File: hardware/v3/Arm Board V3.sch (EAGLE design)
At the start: 75 parts, among them CN1 1X4-BIG, IC1 L6206D, IC2 L6206D, IC3 L6206D, IC4 7812TV, IC5 7812TV, IC6 7812TV, IC7 7812DT, IC9 7812DT, Q3 Q_LTC490, U1 MAX3468CPA, U2 XBEE-1B3

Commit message: Created and populated BOM
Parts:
- C12: device SparkFun-Capacitors:CAPKIT -> SparkFun-Capacitors:0.1UF-25V-5%(0603)
- R9: device SparkFun-Passives:RESISTOR0805-RES -> SparkFun-Passives:RESISTOR0603-RES
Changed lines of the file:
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@@
 <part name="GND53" library="SparkFun-Aesthetics" deviceset="GND" device=""/>
 <part name="GND54" library="SparkFun-Aesthetics" deviceset="GND" device=""/>
-<part name="R9" library="SparkFun-Passives" deviceset="RESISTOR" device="0805-RES" value="220"/>
+<part name="R9" library="SparkFun-Passives" deviceset="RESISTOR" device="0603-RES" value="220"/>
 <part name="U$1" library="StellarisLaunchPad_Fred" deviceset="STELLARIS-LAUNCHPAD" device="STELLARIS-LAUNCHPAD-XL"/>
 <part name="U$3" library="SparkFun-Connectors" deviceset="RJ45-8" device="PTH"/>
@@
 <part name="Q3" library="PCB0M1" deviceset="Q_LTC490" device=""/>
 <part name="R11" library="SparkFun-Passives" deviceset="RESISTOR" device="0603-RES" value="120 Ohm"/>
-<part name="C12" library="SparkFun-Capacitors" deviceset="CAP" device="KIT" value=".1uF"/>
+<part name="C12" library="SparkFun-Capacitors" deviceset="0.1UF-25V-5%(0603)" device="" value=".1uF"/>
 <part name="GND8" library="SparkFun-Aesthetics" deviceset="GND" device=""/>
 <part name="H1" library="Lib_TH" deviceset="H_MNTHOLE" device="_#4"/>

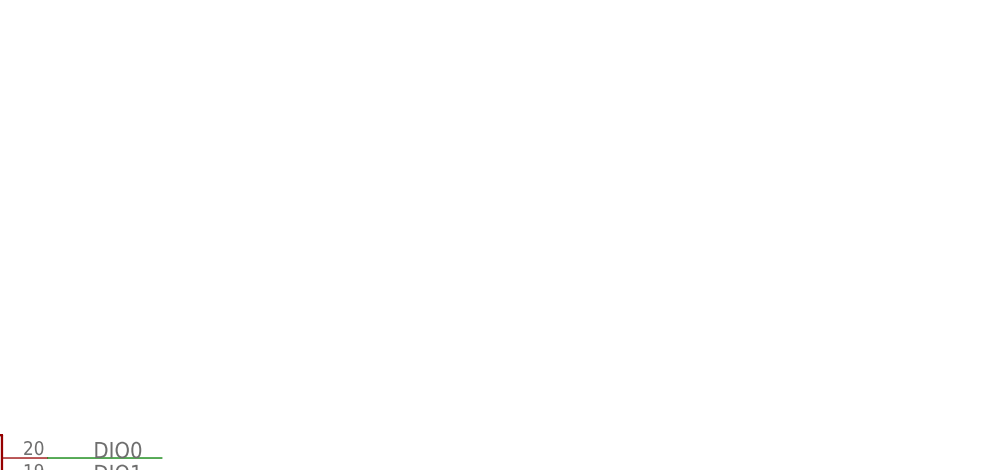
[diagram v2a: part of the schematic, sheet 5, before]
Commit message: Added RS485 jack next to Xbee
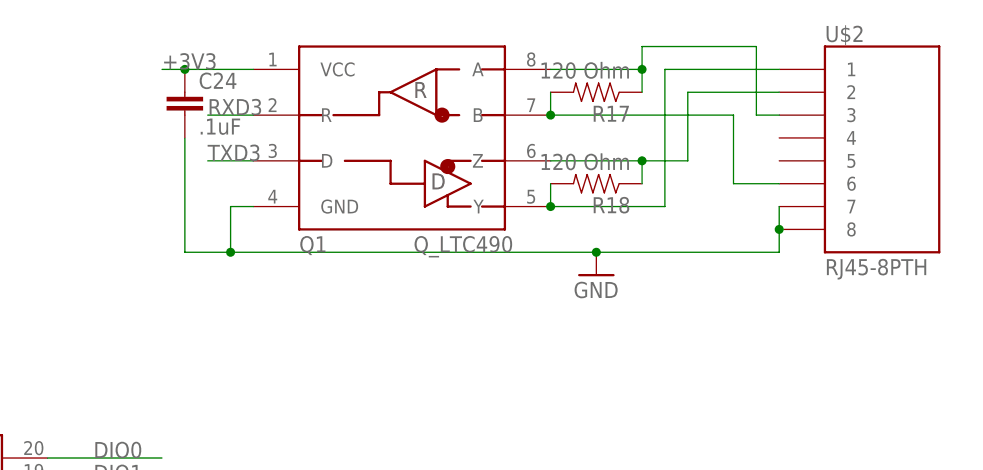
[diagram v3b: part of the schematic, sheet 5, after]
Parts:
- added C24: .1uF, SparkFun-Capacitors:0.1UF-25V-5%(0603)
- added Q1: Q_LTC490, PCB0M1:Q_LTC490
- added R17, R18: 120 Ohm, SparkFun-Passives:RESISTOR0603-RES
- added U$2: RJ45-8PTH, SparkFun-Connectors:RJ45-8PTH
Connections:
- new net N$12: Q1.Y, R18.2, U$2.1
- new net N$14: Q1.Z, R18.1, U$2.2
- new net N$20: Q1.B, R17.2, U$2.6
- new net N$21: Q1.A, R17.1, U$2.3
- net +3V3: now also C24.1, Q1.VCC
- net GND: now also C24.2, Q1.GND, U$2.7, U$2.8
- net RXD3: now also Q1.R
- net TXD3: now also Q1.D
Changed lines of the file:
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@@
 <part name="C23" library="SparkFun-Capacitors" deviceset="0.1UF-25V(+80/-20%)(0603)" device="" value="0.1uF"/>
 <part name="IC9" library="linear" deviceset="78*" device="DT" technology="12" value="7812DT"/>
+<part name="U$2" library="SparkFun-Connectors" deviceset="RJ45-8" device="PTH"/>
+<part name="R17" library="SparkFun-Passives" deviceset="RESISTOR" device="0603-RES" value="120 Ohm"/>
+<part name="GND25" library="supply1" deviceset="GND" device=""/>
+<part name="Q1" library="PCB0M1" deviceset="Q_LTC490" device=""/>
+<part name="R18" library="SparkFun-Passives" deviceset="RESISTOR" device="0603-RES" value="120 Ohm"/>
+<part name="C24" library="SparkFun-Capacitors" deviceset="0.1UF-25V-5%(0603)" device="" value=".1uF"/>
 </parts>
 <sheets>
@@
 <instance part="R16" gate="G$1" x="55.88" y="63.5" rot="R90"/>
 <instance part="GND31" gate="1" x="55.88" y="43.18"/>
+<instance part="U$2" gate="G$1" x="162.56" y="58.42"/>
+<instance part="R17" gate="G$1" x="129.54" y="66.04" rot="R180"/>
+<instance part="GND25" gate="1" x="129.54" y="45.72"/>
+<instance part="Q1" gate="G$1" x="99.06" y="58.42"/>
+<instance part="R18" gate="G$1" x="129.54" y="55.88" rot="R180"/>
+<instance part="C24" gate="G$1" x="83.82" y="63.5"/>
 </instances>
 <busses>
@@
 <wire x1="27.94" y1="2.54" x2="2.54" y2="2.54" width="0.1524" layer="91"/>
 </segment>
+<segment>
+<pinref part="GND25" gate="1" pin="GND"/>
+<wire x1="88.9" y1="48.26" x2="129.54" y2="48.26" width="0.1524" layer="91"/>
+<pinref part="Q1" gate="G$1" pin="GND"/>
+<wire x1="88.9" y1="48.26" x2="88.9" y2="53.34" width="0.1524" layer="91"/>
+<wire x1="88.9" y1="53.34" x2="91.44" y2="53.34" width="0.1524" layer="91"/>
+<junction x="129.54" y="48.26"/>
+<pinref part="C24" gate="G$1" pin="2"/>
+<wire x1="83.82" y1="60.96" x2="83.82" y2="48.26" width="0.1524" layer="91"/>
+<wire x1="83.82" y1="48.26" x2="88.9" y2="48.26" width="0.1524" layer="91"/>
+<junction x="88.9" y="48.26"/>
+<pinref part="U$2" gate="G$1" pin="8"/>
+<pinref part="U$2" gate="G$1" pin="7"/>
+<wire x1="149.86" y1="53.34" x2="149.86" y2="50.8" width="0.1524" layer="91"/>
+<junction x="149.86" y="50.8"/>
+<wire x1="149.86" y1="50.8" x2="149.86" y2="48.26" width="0.1524" layer="91"/>
+<wire x1="129.54" y1="48.26" x2="149.86" y2="48.26" width="0.1524" layer="91"/>
+</segment>
 </net>
 <net name="N$38" class="0">
@@
 <label x="7.62" y="22.86" size="1.778" layer="95"/>
 </segment>
+<segment>
+<pinref part="Q1" gate="G$1" pin="R"/>
+<wire x1="86.36" y1="63.5" x2="91.44" y2="63.5" width="0.1524" layer="91"/>
+<label x="86.36" y="63.5" size="1.778" layer="95"/>
+</segment>
 </net>
 <net name="DIO4" class="0">
@@
 <label x="15.24" y="71.12" size="1.778" layer="95"/>
 </segment>
+<segment>
+<pinref part="Q1" gate="G$1" pin="VCC"/>
+<pinref part="C24" gate="G$1" pin="1"/>
+<wire x1="91.44" y1="68.58" x2="83.82" y2="68.58" width="0.1524" layer="91"/>
+<wire x1="83.82" y1="68.58" x2="81.28" y2="68.58" width="0.1524" layer="91"/>
+<junction x="83.82" y="68.58"/>
+<label x="81.28" y="68.58" size="1.778" layer="95"/>
+</segment>
 </net>
 <net name="TXD3" class="0">
@@
 <label x="15.24" y="45.72" size="1.778" layer="95"/>
 </segment>
+<segment>
+<pinref part="Q1" gate="G$1" pin="D"/>
+<wire x1="86.36" y1="58.42" x2="91.44" y2="58.42" width="0.1524" layer="91"/>
+<label x="86.36" y="58.42" size="1.778" layer="95"/>
+</segment>
 </net>
 <net name="XRESET" class="0">
@@
 </segment>
 </net>
+<net name="N$12" class="0">
+<segment>
+<pinref part="Q1" gate="G$1" pin="Y"/>
+<wire x1="124.46" y1="53.34" x2="137.16" y2="53.34" width="0.1524" layer="91"/>
+<wire x1="137.16" y1="53.34" x2="137.16" y2="68.58" width="0.1524" layer="91"/>
+<pinref part="U$2" gate="G$1" pin="1"/>
+<wire x1="137.16" y1="68.58" x2="149.86" y2="68.58" width="0.1524" layer="91"/>
+<pinref part="R18" gate="G$1" pin="2"/>
+<wire x1="124.46" y1="53.34" x2="124.46" y2="55.88" width="0.1524" layer="91"/>
+<junction x="124.46" y="53.34"/>
+</segment>
+</net>
+<net name="N$14" class="0">
+<segment>
+<pinref part="Q1" gate="G$1" pin="Z"/>
+<wire x1="124.46" y1="58.42" x2="134.62" y2="58.42" width="0.1524" layer="91"/>
+<wire x1="134.62" y1="58.42" x2="139.7" y2="58.42" width="0.1524" layer="91"/>
+<wire x1="139.7" y1="58.42" x2="139.7" y2="66.04" width="0.1524" layer="91"/>
+<pinref part="U$2" gate="G$1" pin="2"/>
+<wire x1="139.7" y1="66.04" x2="149.86" y2="66.04" width="0.1524" layer="91"/>
+<pinref part="R18" gate="G$1" pin="1"/>
+<wire x1="134.62" y1="55.88" x2="134.62" y2="58.42" width="0.1524" layer="91"/>
+<junction x="134.62" y="58.42"/>
+</segment>
+</net>
+<net name="N$20" class="0">
+<segment>
+<pinref part="Q1" gate="G$1" pin="B"/>
+<wire x1="124.46" y1="63.5" x2="144.78" y2="63.5" width="0.1524" layer="91"/>
+<wire x1="144.78" y1="63.5" x2="144.78" y2="55.88" width="0.1524" layer="91"/>
+<pinref part="U$2" gate="G$1" pin="6"/>
+<wire x1="144.78" y1="55.88" x2="149.86" y2="55.88" width="0.1524" layer="91"/>
+<pinref part="R17" gate="G$1" pin="2"/>
+<wire x1="124.46" y1="63.5" x2="124.46" y2="66.04" width="0.1524" layer="91"/>
+<junction x="124.46" y="63.5"/>
+</segment>
+</net>
+<net name="N$21" class="0">
+<segment>
+<pinref part="Q1" gate="G$1" pin="A"/>
+<wire x1="124.46" y1="68.58" x2="134.62" y2="68.58" width="0.1524" layer="91"/>
+<wire x1="134.62" y1="68.58" x2="134.62" y2="71.12" width="0.1524" layer="91"/>
+<wire x1="134.62" y1="71.12" x2="147.32" y2="71.12" width="0.1524" layer="91"/>
+<wire x1="147.32" y1="71.12" x2="147.32" y2="63.5" width="0.1524" layer="91"/>
+<pinref part="U$2" gate="G$1" pin="3"/>
+<wire x1="147.32" y1="63.5" x2="149.86" y2="63.5" width="0.1524" layer="91"/>
+<pinref part="R17" gate="G$1" pin="1"/>
+<wire x1="134.62" y1="66.04" x2="134.62" y2="68.58" width="0.1524" layer="91"/>
+<junction x="134.62" y="68.58"/>
+</segment>
+</net>

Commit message: Added headers for serial in and 2 encoders
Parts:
- added JP7: (no value), SparkFun-Connectors:M03PTH
- added JP8, JP9: (no value), SparkFun-Connectors:M04PTH
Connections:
- new net A0: JP8.3, U$1.PE3
- new net A10: JP9.3, U$1.PB4
- new net A11: JP9.4, U$1.PB5
- new net A7: JP8.4, U$1.PD0
- new net RXD5: JP7.2, U$1.PE4
- new net TXD5: JP7.1, U$1.PE5
- net +5V: now also JP8.2, JP9.2
- net GND: now also JP7.3, JP8.1, JP9.1
- net IN2_A_1: now also U$1.PA2; no longer U$1.PD0
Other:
- note added: "A0 A7 A10 A11"
